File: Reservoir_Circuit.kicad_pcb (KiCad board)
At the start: 2 copper layers, 70 x 57.5 mm, 5 parts, among them J1 CN7, J2 CN10

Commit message: Set up net classes, and added bulk decoupling capacitors and an octal buffer
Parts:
- added C1: 25uF, Capacitor_SMD:C_Elec_3x5.4, B.Cu at (113.5, 72.5)
- added C2: 25uF, Capacitor_SMD:C_Elec_3x5.4, B.Cu at (112.8, 89.5)
- added C3: 10nF, Capacitor_SMD:C_1206_3216Metric, F.Cu at (123.0, 92.0)
- added J3: ECE298_RS_PWR_EXT, Connector_JST:JST_EH_B2B-EH-A_1x02_P2.50mm_Vertical, F.Cu at (116.5, 79.9)
- added U1: CD74HC540E, CD74HC540M:SOIC127P1030X265-20N, F.Cu at (131.5, 87.5)
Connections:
- J1 pad 12: /IOREF -> +3V3
- J1 pad 14: /~{RST} -> unconnected-(J1-Pin_14-Pad14)
- J1 pad 18: +5V -> unconnected-(J1-Pin_18-Pad18)
- J1 pad 24: /VIN -> unconnected-(J1-Pin_24-Pad24)
- J1 pad 33: +BATT -> unconnected-(J1-Pin_33-Pad33)
- J1 pad 5: VDD -> unconnected-(J1-Pin_5-Pad5)
- J1 pad 6: /E5V -> unconnected-(J1-Pin_6-Pad6)
- J2 pad 11: unconnected-(J2-Pin_11-Pad11) -> GND
- J2 pad 32: GNDA -> GND
- J2 pad 8: /5V_USB_CHGR -> unconnected-(J2-Pin_8-Pad8)
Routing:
- net GND: track 0.00 -> 69.6 mm
- net +5V_EXT: track 0.00 -> 32.7 mm
- net +3V3: track 0.00 -> 6.67 mm
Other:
- outline, holes or cut-outs redrawn

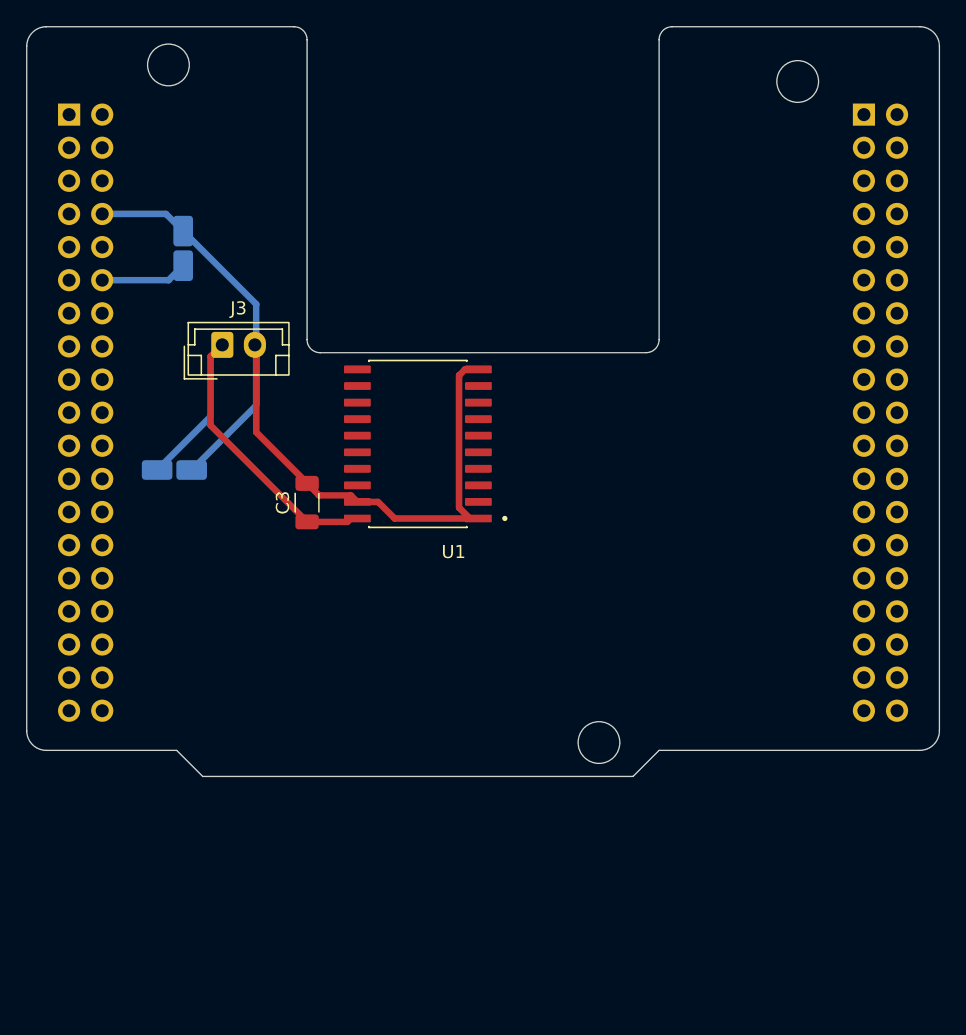
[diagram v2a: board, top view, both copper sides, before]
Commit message: Finished wiring timer board
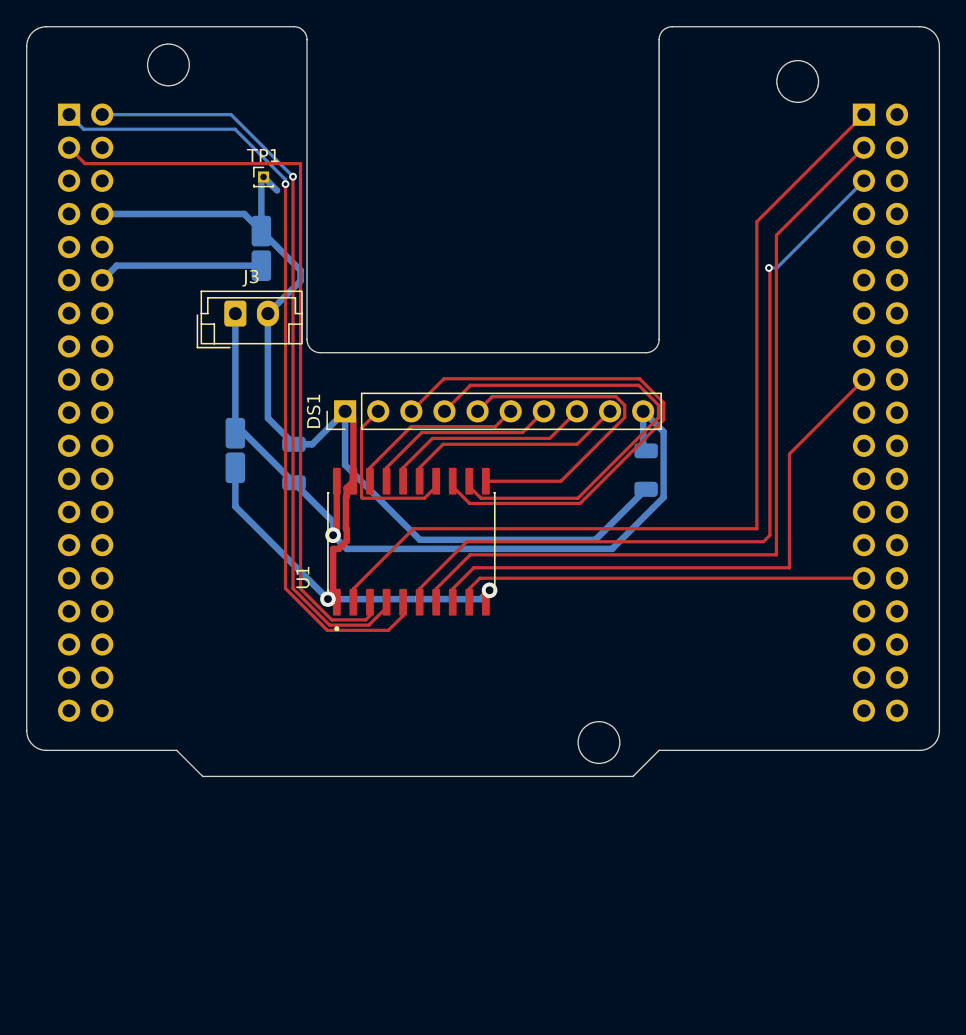
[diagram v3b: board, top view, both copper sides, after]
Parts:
- added C4: 10nF, Capacitor_SMD:C_1206_3216Metric, B.Cu at (149.0, 89.5)
- added DS1: ~, Connector_PinHeader_2.54mm:PinHeader_1x10_P2.54mm_Vertical, F.Cu at (125.9, 85.0)
- added TP1: TP_GND, Connector_PinHeader_1.00mm:PinHeader_1x01_P1.00mm_Vertical, F.Cu at (119.7, 67.0)
- C3: moved to B.Cu
- moved U1 7.52 mm to (131.0, 95.0), turned to 90 degrees
- moved C1 6.00 mm to (119.5, 72.5)
- moved C2 4.91 mm to (117.5, 88.0), turned to -90 degrees
- moved C3 3.16 mm to (122.0, 89.0)
- moved J3 2.60 mm to (117.5, 77.5)
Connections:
- J1 pad 1: unconnected-(J1-Pin_1-Pad1) -> /PC10
- J1 pad 2: unconnected-(J1-Pin_2-Pad2) -> /PC11
- J1 pad 3: unconnected-(J1-Pin_3-Pad3) -> /PC12
- J2 pad 1: unconnected-(J2-Pin_1-Pad1) -> /PC9
- J2 pad 17: unconnected-(J2-Pin_17-Pad17) -> /PB6
- J2 pad 29: unconnected-(J2-Pin_29-Pad29) -> /PB5
- J2 pad 3: unconnected-(J2-Pin_3-Pad3) -> /PB8
- J2 pad 5: unconnected-(J2-Pin_5-Pad5) -> /PB9
- U1 pad 11: unconnected-(U1-~Y7-Pad11) -> /BCD_A0
- U1 pad 12: unconnected-(U1-~Y6-Pad12) -> /BCD_A1
- U1 pad 13: unconnected-(U1-~Y5-Pad13) -> /BCD_A2
- U1 pad 14: unconnected-(U1-~Y4-Pad14) -> /BCD_A3
- U1 pad 15: unconnected-(U1-~Y3-Pad15) -> /BCD_B0
- U1 pad 16: unconnected-(U1-~Y2-Pad16) -> /BCD_B1
- U1 pad 17: unconnected-(U1-~Y1-Pad17) -> /BCD_B2
- U1 pad 18: unconnected-(U1-~Y0-Pad18) -> /BCD_B3
- U1 pad 2: unconnected-(U1-A0-Pad2) -> /PC9
- U1 pad 3: unconnected-(U1-A1-Pad3) -> /PC12
- U1 pad 4: unconnected-(U1-A2-Pad4) -> /PC11
- U1 pad 5: unconnected-(U1-A3-Pad5) -> /PC10
- U1 pad 6: unconnected-(U1-A4-Pad6) -> /PB9
- U1 pad 7: unconnected-(U1-A5-Pad7) -> /PB8
- U1 pad 8: unconnected-(U1-A6-Pad8) -> /PB6
- U1 pad 9: unconnected-(U1-A7-Pad9) -> /PB5
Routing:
- net /PC9: track 0.00 -> 69.0 mm
- net /PB8: track 0.00 -> 62.2 mm
- net /PC10: track 0.00 -> 61.9 mm, vias 0 -> 1
- net /PB9: track 0.00 -> 60.2 mm, vias 0 -> 1
- net /PC12: track 0.00 -> 58.3 mm
- net /PC11: track 0.00 -> 57.5 mm, vias 0 -> 1
- net GND: track 69.6 -> 115.6 mm, vias 0 -> 2
- net /PB6: track 0.00 -> 44.3 mm
- net /BCD_A2: track 0.00 -> 42.2 mm
- net /BCD_A1: track 0.00 -> 36.7 mm
- net /PB5: track 0.00 -> 31.6 mm
- net +5V_EXT: track 32.7 -> 63.0 mm, vias 0 -> 1
- net /BCD_A0: track 0.00 -> 25.6 mm
- net /BCD_B0: track 0.00 -> 17.4 mm
- net /BCD_B1: track 0.00 -> 16.2 mm
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
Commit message: Removed right angles in PCB, updated headers to make DRC happy
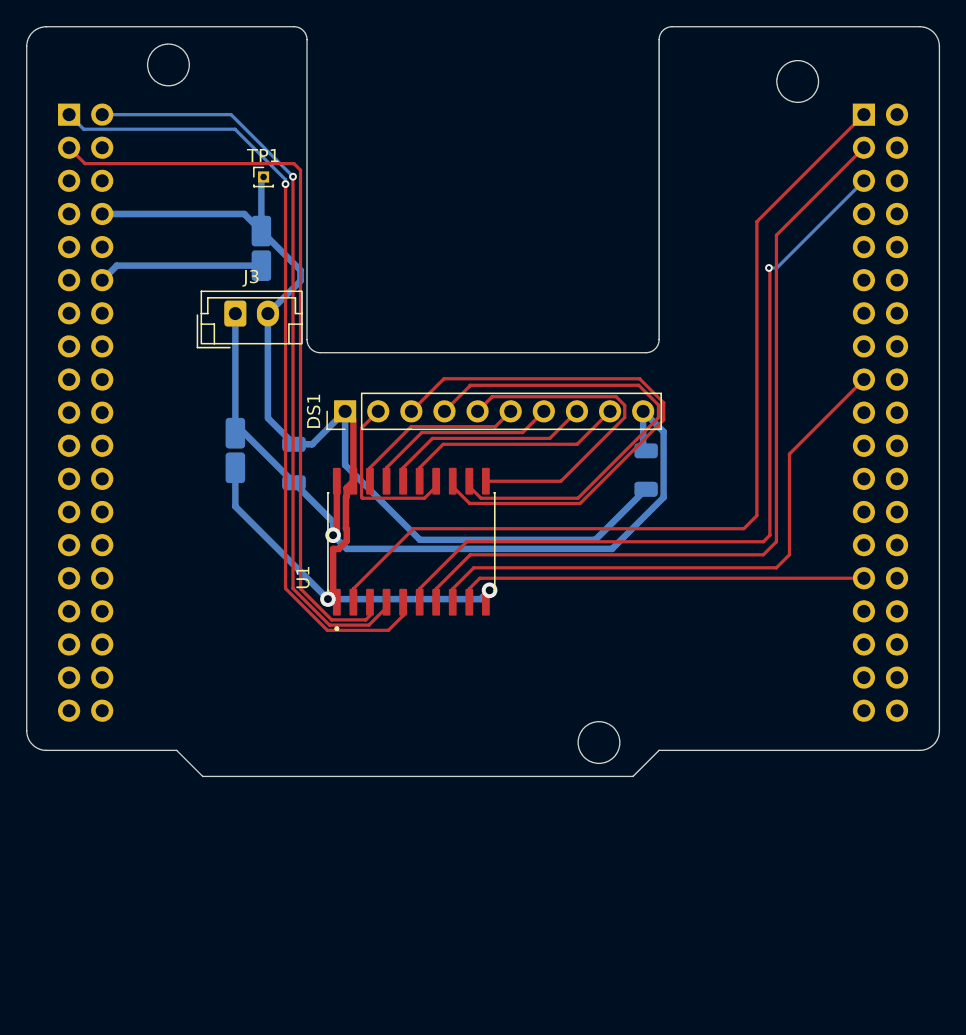
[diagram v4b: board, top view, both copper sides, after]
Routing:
- net GND: track 115.6 -> 114.1 mm
- net /PC9: track 69.0 -> 68.5 mm
- net /PB8: track 62.2 -> 61.6 mm
- net /PB6: track 44.3 -> 43.7 mm

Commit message: Added hardware for ultrasonic sensor
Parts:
- added C5: 10nF, Capacitor_SMD:C_1206_3216Metric, F.Cu at (150.0, 104.0)
- added C6: 10nF, Capacitor_SMD:C_1206_3216Metric, F.Cu at (145.0, 104.0)
- added U2: HC-SR04, HC-SR04:XCVR_HC-SR04, F.Cu at (135.7, 111.5)
- added U3: ~, CD74HC4049MT:SOIC127P600X175-16N, F.Cu at (135.5, 105.5)
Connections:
- J1 pad 30: unconnected-(J1-Pin_30-Pad30) -> /PA1
- J2 pad 2: unconnected-(J2-Pin_2-Pad2) -> /PC8
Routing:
- net /PC8: track 0.00 -> 64.4 mm
- net +3V3: track 12.7 -> 69.1 mm, vias 0 -> 1
- net GND: track 114.1 -> 157.9 mm
- net /PA1: track 0.00 -> 36.2 mm
- net +5V_EXT: track 63.0 -> 96.4 mm, vias 1 -> 2
- net /ECHO: track 0.00 -> 3.72 mm
- net /PB9: track 60.2 -> 61.7 mm

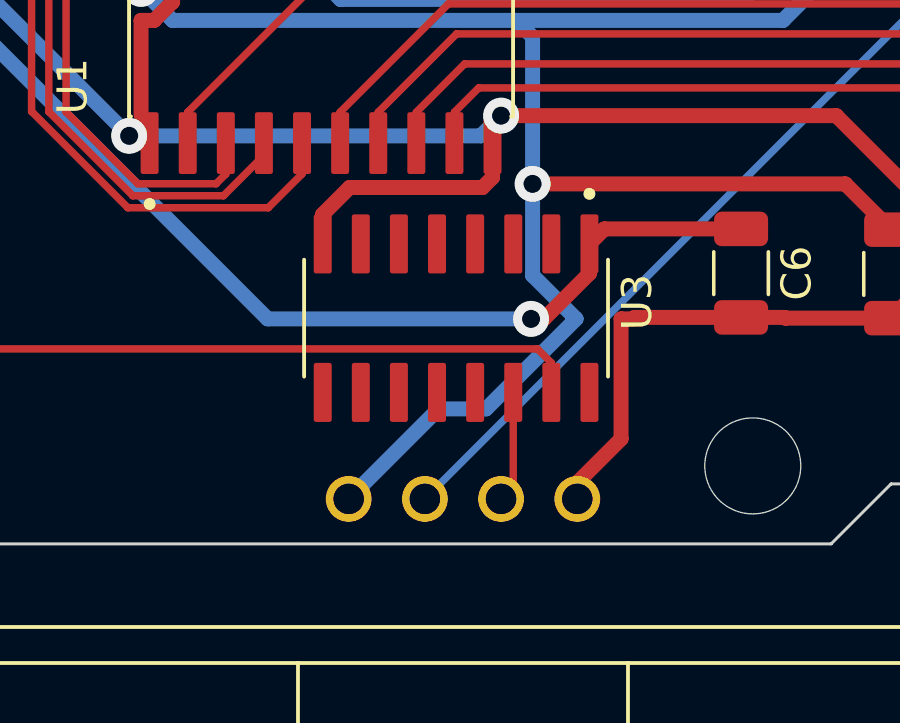
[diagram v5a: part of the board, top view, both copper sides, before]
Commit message: Pulled unused input pins to GND
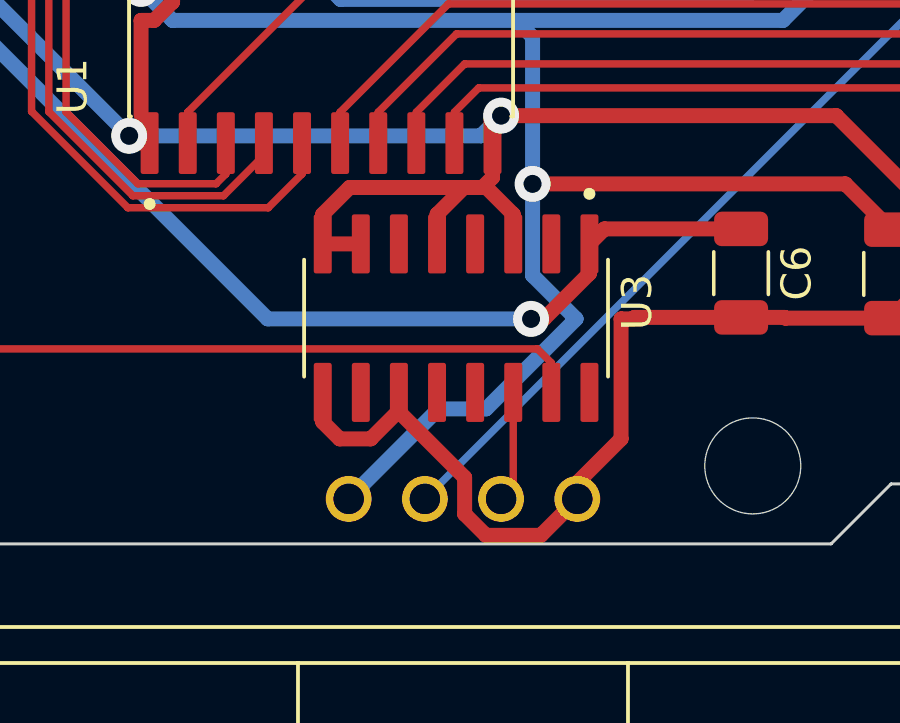
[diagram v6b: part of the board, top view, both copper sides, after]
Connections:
- U3 pad 11: unconnected-(U3-5A-Pad11) -> GND
- U3 pad 3: unconnected-(U3-1A-Pad3) -> GND
- U3 pad 5: unconnected-(U3-2A-Pad5) -> GND
- U3 pad 7: unconnected-(U3-3A-Pad7) -> GND
- U3 pad 9: unconnected-(U3-4A-Pad9) -> GND
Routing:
- net GND: track 157.9 -> 178.7 mm
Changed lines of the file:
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@@
 			(layers "F.Cu" "F.Mask" "F.Paste")
 			(roundrect_rratio 0.125)
-			(net "unconnected-(U3-1A-Pad3)")
+			(net "GND")
 			(pinfunction "1A_3")
-			(pintype "input+no_connect")
+			(pintype "input")
 			(solder_mask_margin 0.102)
 		)
@@
 			(layers "F.Cu" "F.Mask" "F.Paste")
 			(roundrect_rratio 0.125)
-			(net "unconnected-(U3-2A-Pad5)")
+			(net "GND")
 			(pinfunction "2A_5")
-			(pintype "input+no_connect")
+			(pintype "input")
 			(solder_mask_margin 0.102)
 		)
@@
 			(layers "F.Cu" "F.Mask" "F.Paste")
 			(roundrect_rratio 0.125)
-			(net "unconnected-(U3-3A-Pad7)")
+			(net "GND")
 			(pinfunction "3A_7")
-			(pintype "input+no_connect")
+			(pintype "input")
 			(solder_mask_margin 0.102)
 		)
@@
 			(layers "F.Cu" "F.Mask" "F.Paste")
 			(roundrect_rratio 0.125)
-			(net "unconnected-(U3-4A-Pad9)")
+			(net "GND")
 			(pinfunction "4A_9")
-			(pintype "input+no_connect")
+			(pintype "input")
 			(solder_mask_margin 0.102)
 		)
@@
 			(layers "F.Cu" "F.Mask" "F.Paste")
 			(roundrect_rratio 0.125)
-			(net "unconnected-(U3-5A-Pad11)")
+			(net "GND")
 			(pinfunction "5A_11")
-			(pintype "input+no_connect")
+			(pintype "input")
 			(solder_mask_margin 0.102)
 		)
@@
 	(segment
 		(start 131.950001 101.12)
-		(end 136.38 101.12)
+		(end 135.760001 101.12)
 		(width 0.5)
 		(layer "F.Cu")
@@
 	)
 	(segment
+		(start 131.055 103)
+		(end 132.325 103)
+		(width 0.5)
+		(layer "F.Cu")
+		(net "GND")
+	)
+	(segment
 		(start 126.05 94.934925)
 		(end 125.434925 95.55)
@@
 	)
 	(segment
+		(start 133.595 108.595)
+		(end 135.785 110.785)
+		(width 0.5)
+		(layer "F.Cu")
+		(net "GND")
+	)
+	(segment
+		(start 134.865 102.015001)
+		(end 135.760001 101.12)
+		(width 0.5)
+		(layer "F.Cu")
+		(net "GND")
+	)
+	(segment
+		(start 135.785 112.00327)
+		(end 136.49673 112.715)
+		(width 0.5)
+		(layer "F.Cu")
+		(net "GND")
+	)
+	(segment
+		(start 133.595 108.559542)
+		(end 133.595 107.95)
+		(width 0.5)
+		(layer "F.Cu")
+		(net "GND")
+	)
+	(segment
+		(start 136.49673 112.715)
+		(end 138.325 112.715)
+		(width 0.5)
+		(layer "F.Cu")
+		(net "GND")
+	)
+	(segment
+		(start 137.405 103)
+		(end 137.405 102.015001)
+		(width 0.5)
+		(layer "F.Cu")
+		(net "GND")
+	)
+	(segment
 		(start 125.285 99.64)
 		(end 124.845384 99.64)
@@
 	)
 	(segment
+		(start 134.865 103)
+		(end 134.865 102.015001)
+		(width 0.5)
+		(layer "F.Cu")
+		(net "GND")
+	)
+	(segment
+		(start 131.620001 109.5)
+		(end 132.654542 109.5)
+		(width 0.5)
+		(layer "F.Cu")
+		(net "GND")
+	)
+	(segment
 		(start 146.45 105.45)
 		(end 146.475 105.475)
@@
 	)
 	(segment
+		(start 135.760001 101.12)
+		(end 136.38 101.12)
+		(width 0.5)
+		(layer "F.Cu")
+		(net "GND")
+	)
+	(segment
 		(start 126.05 94.065075)
 		(end 126.05 94.934925)
@@
 	)
 	(segment
+		(start 131.055 107.95)
+		(end 131.055 108.934999)
+		(width 0.5)
+		(layer "F.Cu")
+		(net "GND")
+	)
+	(segment
 		(start 146.475 105.475)
 		(end 150 105.475)
@@
 	)
 	(segment
+		(start 132.654542 109.5)
+		(end 133.595 108.559542)
+		(width 0.5)
+		(layer "F.Cu")
+		(net "GND")
+	)
+	(segment
 		(start 125 95.55)
 		(end 125 98.700458)
@@
 	)
 	(segment
+		(start 135.785 110.785)
+		(end 135.785 112.00327)
+		(width 0.5)
+		(layer "F.Cu")
+		(net "GND")
+	)
+	(segment
+		(start 137.405 102.015001)
+		(end 136.509999 101.12)
+		(width 0.5)
+		(layer "F.Cu")
+		(net "GND")
+	)
+	(segment
 		(start 136.715 100.785)
 		(end 136.715 99.64)
@@
 	)
 	(segment
+		(start 133.595 107.95)
+		(end 133.595 108.595)
+		(width 0.5)
+		(layer "F.Cu")
+		(net "GND")
+	)
+	(segment
 		(start 148.171878 98.725)
 		(end 137 98.725)
@@
 	)
 	(segment
+		(start 138.325 112.715)
+		(end 139.54 111.5)
+		(width 0.5)
+		(layer "F.Cu")
+		(net "GND")
+	)
+	(segment
 		(start 141.45 105.45)
 		(end 141.4 105.5)
@@
 	)
 	(segment
+		(start 131.055 108.934999)
+		(end 131.620001 109.5)
+		(width 0.5)
+		(layer "F.Cu")
+		(net "GND")
+	)
+	(segment
 		(start 126.555 90.36)
 		(end 126.555 85.635)
 		(width 0.5)
 		(layer "F.Cu")
+		(net "GND")
+	)
+	(segment
+		(start 136.509999 101.12)
+		(end 135.760001 101.12)
+		(width 0.5)
+		(layer "F.Cu")
